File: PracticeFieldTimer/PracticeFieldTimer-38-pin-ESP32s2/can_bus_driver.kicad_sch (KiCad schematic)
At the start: 5 parts, among them U2 SN65HVD230DR

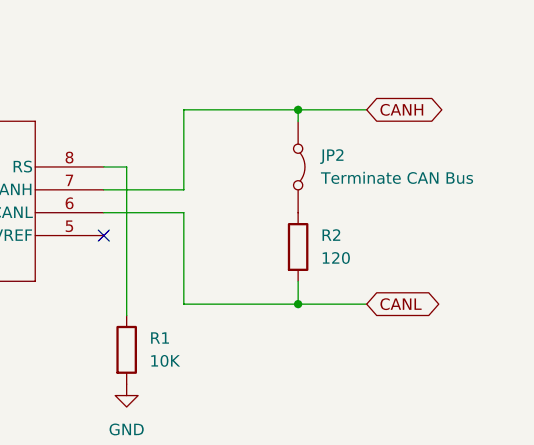
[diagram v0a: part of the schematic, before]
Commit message: Clean up and assign most footprints. Need footprint for decoupling capacitor.
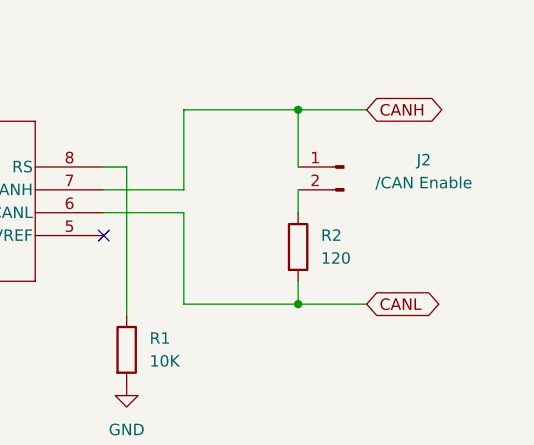
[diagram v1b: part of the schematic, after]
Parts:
- removed JP2: Terminate CAN Bus, symbol Jumper:Jumper_2_Bridged
- added J2: /CAN Enable, Connector_PinHeader_2.54mm:PinHeader_1x02_P2.54mm_Vertical, symbol Connector:Conn_01x02_Pin
- R1, R2: footprint (none) -> Resistor_THT:R_Axial_DIN0414_L11.9mm_D4.5mm_P5.08mm_Vertical
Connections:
- net CANH: now also J2.1 (Pin_1)
- net at R2.1: now also J2.2 (Pin_2)
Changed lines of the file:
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@@
+	)
+	(junction
+		(at 201.93 95.25)
+		(diameter 0)
+		(color 0 0 0 0)
 	)
 	(junction
@@
 		(color 0 0 0 0)
 	)
-	(junction
-		(at 201.93 95.25)
-		(diameter 0)
-		(color 0 0 0 0)
-	)
 	(no_connect
 		(at 180.34 87.63)
@@
 	(wire
 		(pts
+			(xy 201.93 73.66) (xy 209.55 73.66)
+		)
+		(stroke
+			(width 0)
+			(type default)
+		)
+	)
+	(wire
+		(pts
 			(xy 201.93 95.25) (xy 209.55 95.25)
 		)
@@
 	(wire
 		(pts
+			(xy 201.93 82.55) (xy 201.93 85.09)
+		)
+		(stroke
+			(width 0)
+			(type default)
+		)
+	)
+	(wire
+		(pts
 			(xy 189.23 73.66) (xy 201.93 73.66)
 		)
@@
 	(wire
 		(pts
-			(xy 201.93 73.66) (xy 209.55 73.66)
-		)
-		(stroke
-			(width 0)
-			(type default)
-		)
-	)
-	(wire
-		(pts
 			(xy 189.23 85.09) (xy 189.23 95.25)
 		)
@@
 	(wire
 		(pts
-			(xy 201.93 74.93) (xy 201.93 73.66)
-		)
-		(stroke
-			(width 0)
-			(type default)
-		)
-	)
-	(wire
-		(pts
 			(xy 102.87 85.09) (xy 124.46 85.09)
 		)
@@
 		(pts
 			(xy 182.88 80.01) (xy 182.88 96.52)
+		)
+		(stroke
+			(width 0)
+			(type default)
+		)
+	)
+	(wire
+		(pts
+			(xy 201.93 73.66) (xy 201.93 80.01)
 		)
 		(stroke
@@
 				(justify right)
 				(hide yes)
-			)
-		)
-	)
-	(symbol
-		(lib_id "Jumper:Jumper_2_Bridged")
-		(at 201.93 80.01 270)
-		(unit 1)
-		(exclude_from_sim no)
-		(in_bom yes)
-		(on_board yes)
-		(dnp no)
-		(fields_autoplaced yes)
-		(property "Reference" "JP2"
-			(at 204.47 78.7399 90)
-			(effects
-				(font
-					(size 1.27 1.27)
-				)
-				(justify left)
-			)
-		)
-		(property "Value" "Terminate CAN Bus"
-			(at 204.47 81.2799 90)
-			(effects
-				(font
-					(size 1.27 1.27)
-				)
-				(justify left)
-			)
-		)
-		(property "Footprint" ""
-			(at 201.93 80.01 0)
-			(effects
-				(font
-					(size 1.27 1.27)
-				)
-				(hide yes)
-			)
-		)
-		(property "Datasheet" "~"
-			(at 201.93 80.01 0)
-			(effects
-				(font
-					(size 1.27 1.27)
-				)
-				(hide yes)
-			)
-		)
-		(property "Description" "Jumper, 2-pole, closed/bridged"
-			(at 201.93 80.01 0)
-			(effects
-				(font
-					(size 1.27 1.27)
-				)
-				(hide yes)
-			)
-		)
-		(pin "2"
-		)
-		(pin "1"
-		)
-		(instances
-			(project ""
-				(path "/845ef731-c8e5-4e97-892b-a237541c6d77/c59ecbc7-edb5-417c-b0b4-a62a3517c5c8"
-					(reference "JP2")
-					(unit 1)
-				)
 			)
 		)
@@
 			)
 		)
-		(property "Footprint" ""
+		(property "Footprint" "Resistor_THT:R_Axial_DIN0414_L11.9mm_D4.5mm_P5.08mm_Vertical"
 			(at 200.152 88.9 90)
 			(effects
@@
 				(path "/845ef731-c8e5-4e97-892b-a237541c6d77/c59ecbc7-edb5-417c-b0b4-a62a3517c5c8"
 					(reference "R2")
+					(unit 1)
+				)
+			)
+		)
+	)
+	(symbol
+		(lib_id "Connector:Conn_01x02_Pin")
+		(at 207.01 80.01 0)
+		(mirror y)
+		(unit 1)
+		(exclude_from_sim no)
+		(in_bom yes)
+		(on_board yes)
+		(dnp no)
+		(property "Reference" "J2"
+			(at 215.9 79.248 0)
+			(effects
+				(font
+					(size 1.27 1.27)
+				)
+			)
+		)
+		(property "Value" "/CAN Enable"
+			(at 215.9 81.788 0)
+			(effects
+				(font
+					(size 1.27 1.27)
+				)
+			)
+		)
+		(property "Footprint" "Connector_PinHeader_2.54mm:PinHeader_1x02_P2.54mm_Vertical"
+			(at 207.01 80.01 0)
+			(effects
+				(font
+					(size 1.27 1.27)
+				)
+				(hide yes)
+			)
+		)
+		(property "Datasheet" "~"
+			(at 207.01 80.01 0)
+			(effects
+				(font
+					(size 1.27 1.27)
+				)
+				(hide yes)
+			)
+		)
+		(property "Description" "Generic connector, single row, 01x02, script generated"
+			(at 207.01 80.01 0)
+			(effects
+				(font
+					(size 1.27 1.27)
+				)
+				(hide yes)
+			)
+		)
+		(pin "2"
+		)
+		(pin "1"
+		)
+		(instances
+			(project "PracticeFieldTimer-38-pin-ESP32s2"
+				(path "/845ef731-c8e5-4e97-892b-a237541c6d77/c59ecbc7-edb5-417c-b0b4-a62a3517c5c8"
+					(reference "J2")
 					(unit 1)
 				)
@@
 			)
 		)
-		(property "Footprint" ""
+		(property "Footprint" "Resistor_THT:R_Axial_DIN0414_L11.9mm_D4.5mm_P5.08mm_Vertical"
 			(at 181.102 100.33 90)
 			(effects

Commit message: Finish filling in footprints.
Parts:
- C1: footprint (none) -> Capacitor_THT:C_Disc_D5.0mm_W2.5mm_P5.00mm
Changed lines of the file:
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@@
 			)
 		)
-		(property "Footprint" ""
+		(property "Footprint" "Capacitor_THT:C_Disc_D5.0mm_W2.5mm_P5.00mm"
 			(at 103.8352 92.71 0)
 			(effects
@@
 			)
 		)
-		(property "Datasheet" "~"
+		(property "Datasheet" "https://www.taydaelectronics.com/10-x-0-1uf-50v-ceramic-disc-capacitor-pkg-of-10.html"
 			(at 102.87 88.9 0)
 			(effects

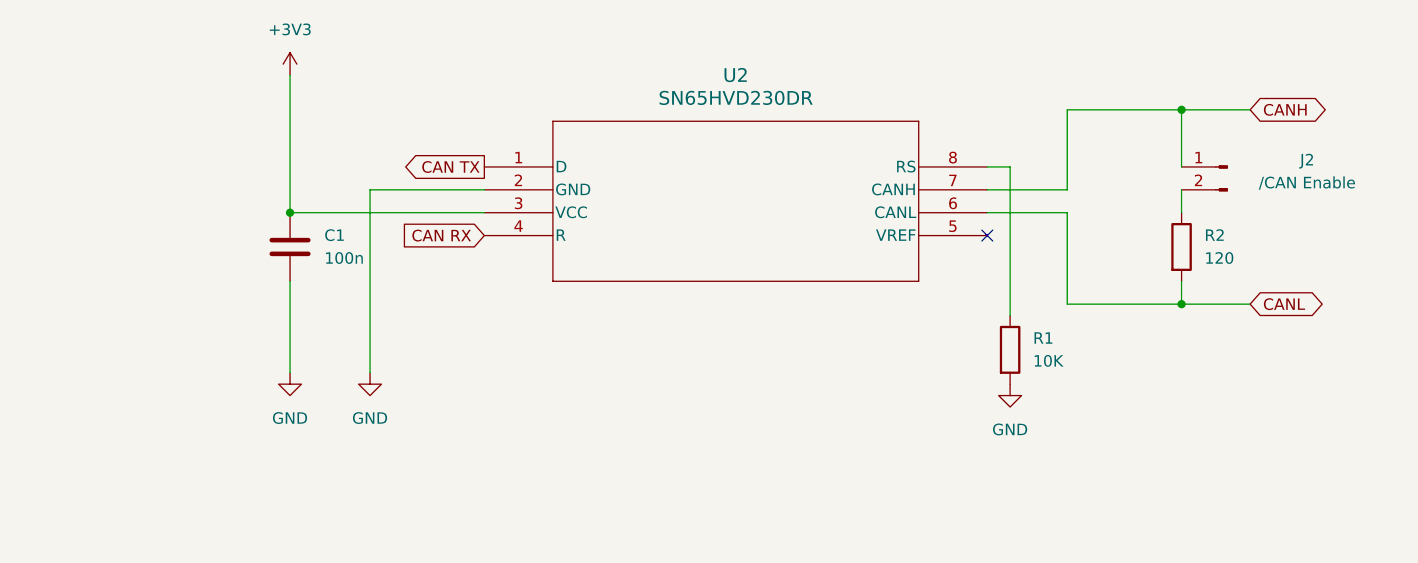
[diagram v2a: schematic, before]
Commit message: Resolved most errors. Still need to add mounting holes and define the board boundary. Also, the I2C header is way too close to the LCD and need to move. The required changes are unclear.
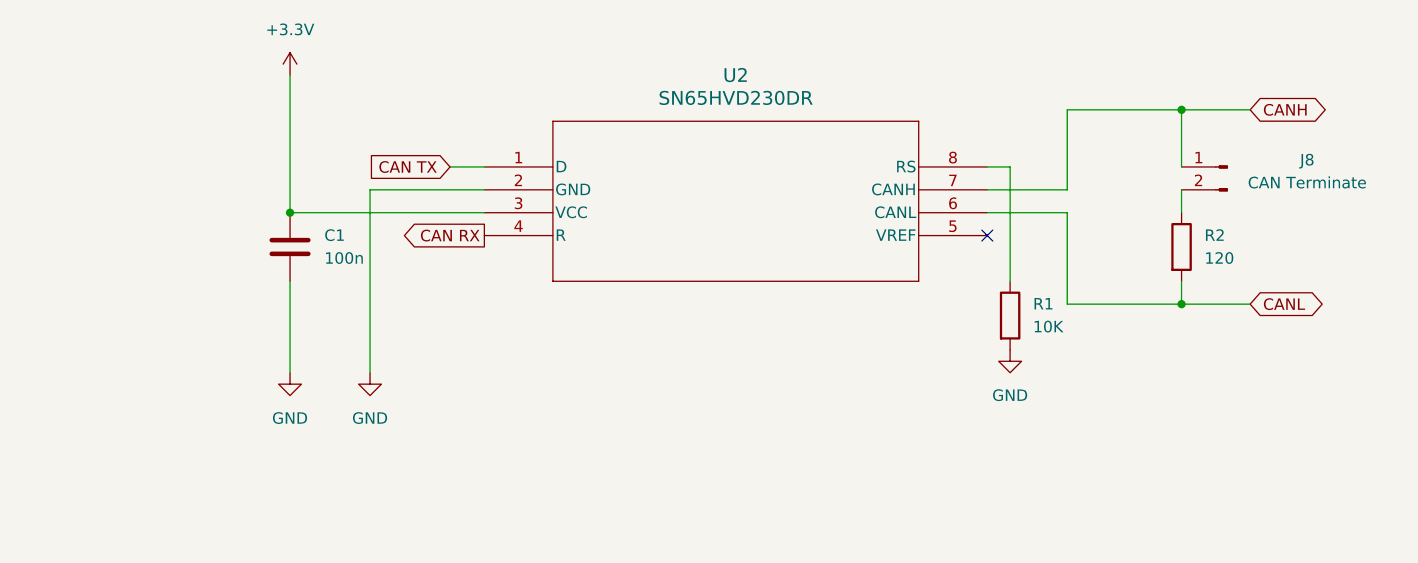
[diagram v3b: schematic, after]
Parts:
- J8: renamed from J2; value /CAN Enable -> CAN Terminate
- R1, R2: footprint Resistor_THT:R_Axial_DIN0414_L11.9mm_D4.5mm_P5.08mm_Vertical -> Resistor_THT:R_Axial_DIN0207_L6.3mm_D2.5mm_P15.24mm_Horizontal
- U2: footprint D8 -> Package_SO:SOIC-8-1EP_3.9x4.9mm_P1.27mm_EP2.514x3.2mm
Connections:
- net +3V3 renamed +3.3V

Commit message: Set schematic size to US Letter and adjust placements to fit. Add copyright notice and team logo.
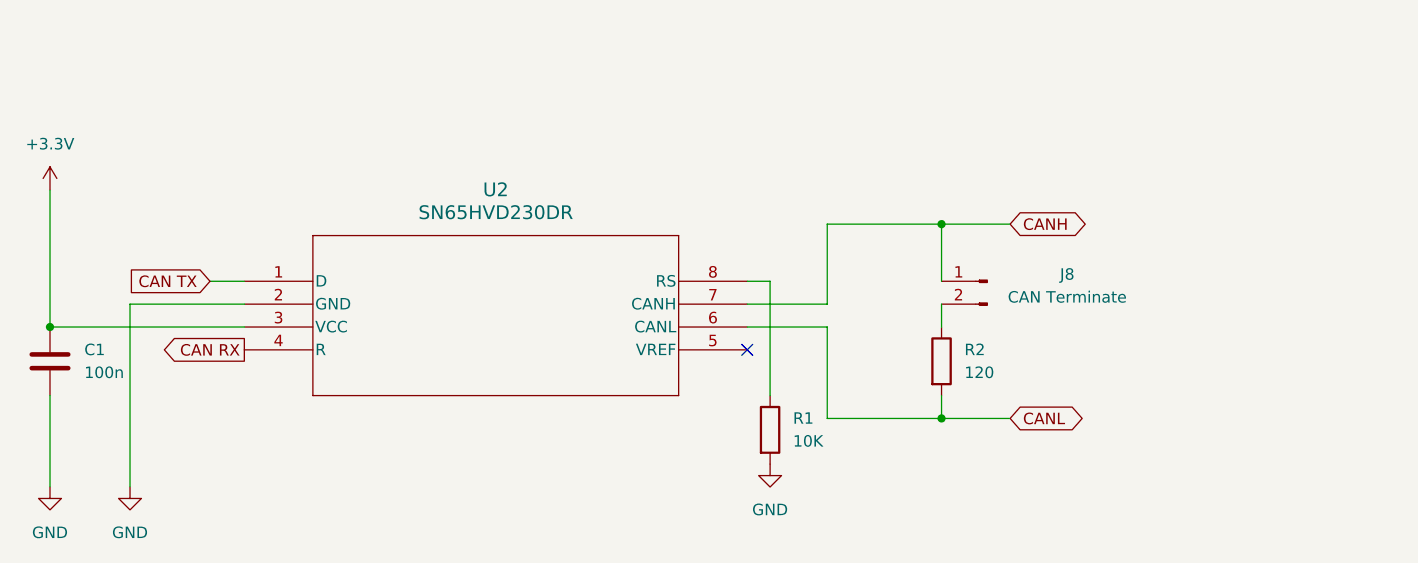
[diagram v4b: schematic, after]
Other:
- moved on the sheet: C1, J8, R1, R2, U2
